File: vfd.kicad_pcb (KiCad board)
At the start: 2 copper layers, 100 x 34 mm, 45 parts, among them J1 I2C_IN, J2 I2C_OUT, Q1 BC857, Q2 BC847, Q3 BC857, Q4 BC847, U1 AP3012, U2 CH32V003F4U6, U3 AP3012, U4 74HCT541PW

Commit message: v0.2
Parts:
- removed TP5, TP6, TP7, TP8, TP9: TestPoint, TestPoint:TestPoint_Pad_D1.5mm
- added D3: LED, vfd:LED_0603_1608Metric, B.Cu at (19.0, 3.40)
- added JP1: A0, vfd:SolderJumper-2_P1.3mm_Open_TrianglePad1.0x1.5mm, B.Cu at (22.4, 7.35)
- added JP2: A1, vfd:SolderJumper-2_P1.3mm_Open_TrianglePad1.0x1.5mm, B.Cu at (25.0, 7.35)
- added JP3: A2, vfd:SolderJumper-2_P1.3mm_Open_TrianglePad1.0x1.5mm, B.Cu at (27.6, 7.35)
- added JP4: A3, vfd:SolderJumper-2_P1.3mm_Open_TrianglePad1.0x1.5mm, B.Cu at (30.1, 7.35)
- added JP5: A4, vfd:SolderJumper-2_P1.3mm_Open_TrianglePad1.0x1.5mm, B.Cu at (32.6, 7.35)
- added N2: OSHW, Symbol:OSHW-Logo_5.7x6mm_SilkScreen, B.Cu at (-40.0, 4.00)
- C1, C2, C3, C4, C5, C6: footprint Capacitor_SMD:C_0603_1608Metric -> vfd:C_0603_1608Metric
- D1, D2: footprint Diode_SMD:D_SOD-323 -> vfd:D_SOD-323
- J1, J2: footprint qwiic:1X04_1MM_RA_GND -> vfd:1X04_1MM_RA_GND
- L1, L2: footprint power-circuit:Inductor_MSC20FC -> vfd:Inductor_MSC20FC
- N1: value Housing -> Logo; footprint footprints:logo_nicolai -> vfd:logo_nicolai
- Q1, Q2, Q3, Q4: footprint Package_TO_SOT_SMD:SOT-23 -> vfd:SOT-23
- R1, R10, R11, R12, R13, R14, R2, R3, R4, R6, R8, R9: footprint Resistor_SMD:R_0603_1608Metric -> vfd:R_0603_1608Metric
- R5: value 1k -> 270; footprint Resistor_SMD:R_0603_1608Metric -> vfd:R_0603_1608Metric
- R7: value 92k82 -> 91k; footprint Resistor_SMD:R_0603_1608Metric -> vfd:R_0603_1608Metric
- TP1, TP2, TP3, TP4: footprint TestPoint:TestPoint_Pad_D1.5mm -> vfd:TestPoint_Pad_D1.5mm
- U1, U3: footprint Package_TO_SOT_SMD:SOT-23-5 -> vfd:SOT-23-5
- U2: footprint Package_DFN_QFN:QFN-20-1EP_3x3mm_P0.4mm_EP1.65x1.65mm -> vfd:QFN-20-1EP_3x3mm_P0.4mm_EP1.65x1.65mm
- U4: footprint Package_SO:TSSOP-20_4.4x6.5mm_P0.65mm -> vfd:TSSOP-20_4.4x6.5mm_P0.65mm
- U5: footprint hcs-12ss59t:HCS-12SS59T -> vfd:HCS-12SS59T
- moved J2 90.7 mm to (45.0, 6.62), turned to -90 degrees
- moved J1 90.4 mm to (45.0, -3.38), turned to -90 degrees
- moved R2 83.4 mm to (41.9, 3.95), turned to 180 degrees
- moved R1 81.9 mm to (41.9, 6.38), turned to 180 degrees
- moved C2 81.0 mm to (41.9, 2.40), turned to 180 degrees
- moved Q1 80.9 mm to (-39.9, -6.38)
- moved Q2 80.9 mm to (-43.9, -6.38)
- moved R10 80.9 mm to (-43.9, -3.38)
- moved R9 80.9 mm to (-39.9, -3.38)
- moved Q3 77.8 mm to (41.8, -6.40)
- moved Q4 77.8 mm to (37.8, -6.40)
- moved R12 77.8 mm to (40.3, -3.40)
- moved R13 77.8 mm to (36.6, -3.40)
- moved U2 72.0 mm to (37.0, 5.00), turned to -90 degrees
- moved R11 67.8 mm to (32.9, 2.27)
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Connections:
- Q1 pad 2: F+ -> +5V
- Q1 pad 3: +5V -> F+
- Q3 pad 2: F- -> +5V
- Q3 pad 3: +5V -> F-
- R5 pad 1: ~{CPU_RST} -> Net-(D3-A)
- R5 pad 2: +3.3V -> Net-(U2-PD7)
- U2 pad 1: ~{CPU_RST} -> Net-(U2-PD7)
- U4 pad 13: ~{CS} -> DIN
- U4 pad 14: ~{RST} -> CLK
- U4 pad 15: CLK -> ~{CS}
- U4 pad 16: DIN -> ~{RST}
- U4 pad 17: CLK_B -> CLK_A
- U4 pad 18: CLK_A -> CLK_B
- U4 pad 2: CLK_A_LV -> CLK_B_LV
- U4 pad 3: CLK_B_LV -> CLK_A_LV
- U4 pad 4: DIN_LV -> ~{RST_LV}
- U4 pad 5: CLK_LV -> ~{CS_LV}
- U4 pad 6: ~{RST_LV} -> CLK_LV
- U4 pad 7: ~{CS_LV} -> DIN_LV
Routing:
- net Net-(U2-PC7): track 34.6 -> 3.94 mm, vias 2 -> 0
- net +5V: track 123.3 -> 99.8 mm, vias 2 -> 4
- net SWIO: track 26.9 -> 4.05 mm
- net DIN_LV: track 7.92 -> 27.6 mm, vias 0 -> 2
- net Net-(JP5-A): track 22.0 -> 3.24 mm
- net CLK_LV: track 8.69 -> 25.9 mm, vias 0 -> 2
- net Net-(U2-PD7): track 0.00 -> 16.0 mm, vias 0 -> 2
- net ~{RST_LV}: track 9.45 -> 24.8 mm, vias 0 -> 2
- net Net-(JP4-A): track 18.7 -> 5.96 mm
- net 24V_ENABLE: track 47.2 -> 57.0 mm
- net ~{CS_LV}: track 15.6 -> 24.0 mm
- net CLK_A: track 83.9 -> 76.0 mm, vias 2 -> 0
- net DIN: track 11.9 -> 4.12 mm
- net CLK: track 12.2 -> 4.68 mm
- net Net-(JP3-A): track 15.6 -> 8.67 mm
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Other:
- board text added: "0 1 2 3 4"
- board text added: "Address"
- board text added: "G + E P"
- board text added: "HCS-12SS59T VFD DISPLAY"
- board text added: "https://product.nicolaielectronics.nl/hcs12ss59t"
- board text removed: "HCS-12SS59T VFD DISPLAY REV 0.1 7-2023"

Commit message: Version 0.2 final
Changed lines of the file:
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@@
     (tags "resistor")
     (property "Reference" "R5" (at 0 1.43 0 unlocked) (layer "B.SilkS")
-      (effects (font (size 1 1) (thickness 0.15)) (justify mirror))
+      (effects (font (size 0.8 0.8) (thickness 0.15)) (justify mirror))
     )
     (property "Value" "270" (at 0 -1.43 180 unlocked) (layer "B.Fab")
@@
     (fp_line (start 0.8 0.4125) (end -0.8 0.4125)
       (stroke (width 0.1) (type solid)) (layer "B.Fab"))
-    (fp_text user "${REFERENCE}" (at 0 0 360) (layer "B.Fab")
+    (fp_text user "${REFERENCE}" (at 0 0 0) (layer "B.Fab")
       (effects (font (size 0.4 0.4) (thickness 0.06)) (justify mirror))
     )
@@
     (descr "SOT, 3 Pin (https://www.jedec.org/system/files/docs/to-236h.pdf variant AB), generated with kicad-footprint-generator ipc_gullwing_generator.py")
     (tags "SOT TO_SOT_SMD")
-    (property "Reference" "Q1" (at 2.7 0 90) (layer "B.SilkS")
+    (property "Reference" "Q1" (at -0.075 -2.325 180) (layer "B.SilkS")
       (effects (font (size 0.8 0.8) (thickness 0.15)) (justify mirror))
     )
@@
     (descr "TSSOP, 20 Pin (JEDEC MO-153 Var AC https://www.jedec.org/document_search?search_api_views_fulltext=MO-153), generated with kicad-footprint-generator ipc_gullwing_generator.py")
     (tags "TSSOP SO")
-    (property "Reference" "U4" (at 0 4.2 -90 unlocked) (layer "B.SilkS")
+    (property "Reference" "U4" (at 0 4.2 90 unlocked) (layer "B.SilkS")
       (effects (font (size 0.8 0.8) (thickness 0.15)) (justify mirror))
     )
@@
     (descr "QFN, 20 Pin (https://www.analog.com/media/en/technical-documentation/data-sheets/3553fc.pdf#page=34), generated with kicad-footprint-generator ipc_noLead_generator.py")
     (tags "QFN NoLead")
-    (property "Reference" "U2" (at 0 2.82 90) (layer "B.SilkS")
+    (property "Reference" "U2" (at 0 -2.8 -90) (layer "B.SilkS")
       (effects (font (size 0.8 0.8) (thickness 0.15)) (justify mirror))
     )
@@
     (tags "Logo OSHW")
     (property "Reference" "N2" (at 0 0 0 unlocked) (layer "B.SilkS") hide
-      (effects (font (size 1 1) (thickness 0.15)) (justify mirror))
+      (effects (font (size 0.8 0.8) (thickness 0.15)) (justify mirror))
     )
     (property "Value" "OSHW" (at 0.75 0 0 unlocked) (layer "B.Fab") hide
@@
     (tags "LED")
     (property "Reference" "D3" (at 0 1.43 0 unlocked) (layer "B.SilkS")
-      (effects (font (size 1 1) (thickness 0.15)) (justify mirror))
+      (effects (font (size 0.8 0.8) (thickness 0.15)) (justify mirror))
     )
     (property "Value" "LED" (at 0 -1.43 180 unlocked) (layer "B.Fab")
@@
     (fp_line (start 0.8 0.4) (end 0.8 -0.4)
       (stroke (width 0.1) (type solid)) (layer "B.Fab"))
-    (fp_text user "${REFERENCE}" (at 0 0 360) (layer "B.Fab")
+    (fp_text user "${REFERENCE}" (at 0 0 0) (layer "B.Fab")
       (effects (font (size 0.4 0.4) (thickness 0.06)) (justify mirror))
     )
@@
     (descr "SOT, 3 Pin (https://www.jedec.org/system/files/docs/to-236h.pdf variant AB), generated with kicad-footprint-generator ipc_gullwing_generator.py")
     (tags "SOT TO_SOT_SMD")
-    (property "Reference" "Q2" (at -2.825 0 90) (layer "B.SilkS")
+    (property "Reference" "Q2" (at 0.025 -2.225 0) (layer "B.SilkS")
       (effects (font (size 0.8 0.8) (thickness 0.15)) (justify mirror))
     )
@@
     (descr "SOT, 3 Pin (https://www.jedec.org/system/files/docs/to-236h.pdf variant AB), generated with kicad-footprint-generator ipc_gullwing_generator.py")
     (tags "SOT TO_SOT_SMD")
-    (property "Reference" "Q3" (at 2.34 2.38 0) (layer "B.SilkS")
+    (property "Reference" "Q3" (at -0.025 -2.3 0) (layer "B.SilkS")
       (effects (font (size 0.8 0.8) (thickness 0.15)) (justify mirror))
     )
@@
     (descr "SOT, 3 Pin (https://www.jedec.org/system/files/docs/to-236h.pdf variant AB), generated with kicad-footprint-generator ipc_gullwing_generator.py")
     (tags "SOT TO_SOT_SMD")
-    (property "Reference" "Q4" (at -2.85 -1.875 0) (layer "B.SilkS")
+    (property "Reference" "Q4" (at -0.025 -2.3 0) (layer "B.SilkS")
       (effects (font (size 0.8 0.8) (thickness 0.15)) (justify mirror))
     )
@@
   (via (at 13.15 4.1) (size 0.6) (drill 0.3) (layers "F.Cu" "B.Cu") (free) (net 29))
   (via (at -48 -14.8) (size 3.5) (drill 3) (layers "F.Cu" "B.Cu") (free) (net 29))
-  (via (at -43.175 -8.525) (size 0.6) (drill 0.3) (layers "F.Cu" "B.Cu") (free) (net 29))
+  (via (at -45.2 -8.7) (size 0.6) (drill 0.3) (layers "F.Cu" "B.Cu") (free) (net 29))
   (via (at 1 4.425) (size 0.6) (drill 0.3) (layers "F.Cu" "B.Cu") (free) (net 29))
   (via (at -9.4 -10.5) (size 0.6) (drill 0.3) (layers "F.Cu" "B.Cu") (free) (net 29))

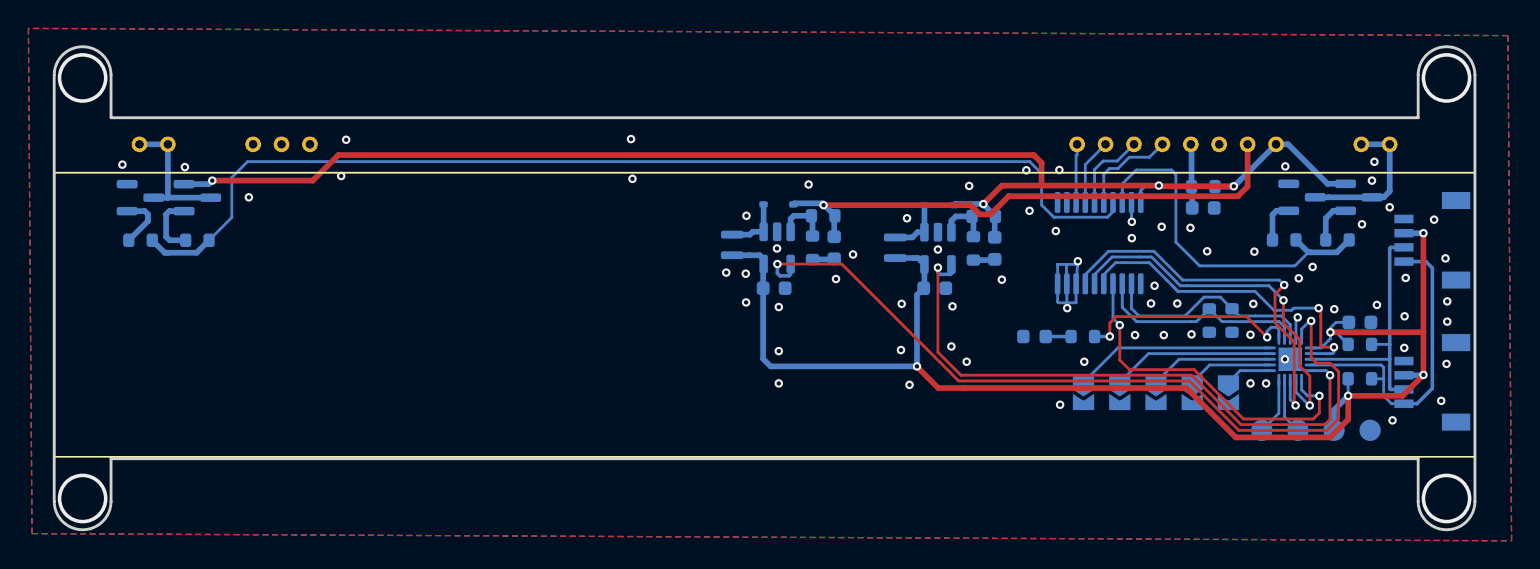
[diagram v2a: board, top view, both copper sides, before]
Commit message: Make inductor pads bigger, make vfd pads and holes larger
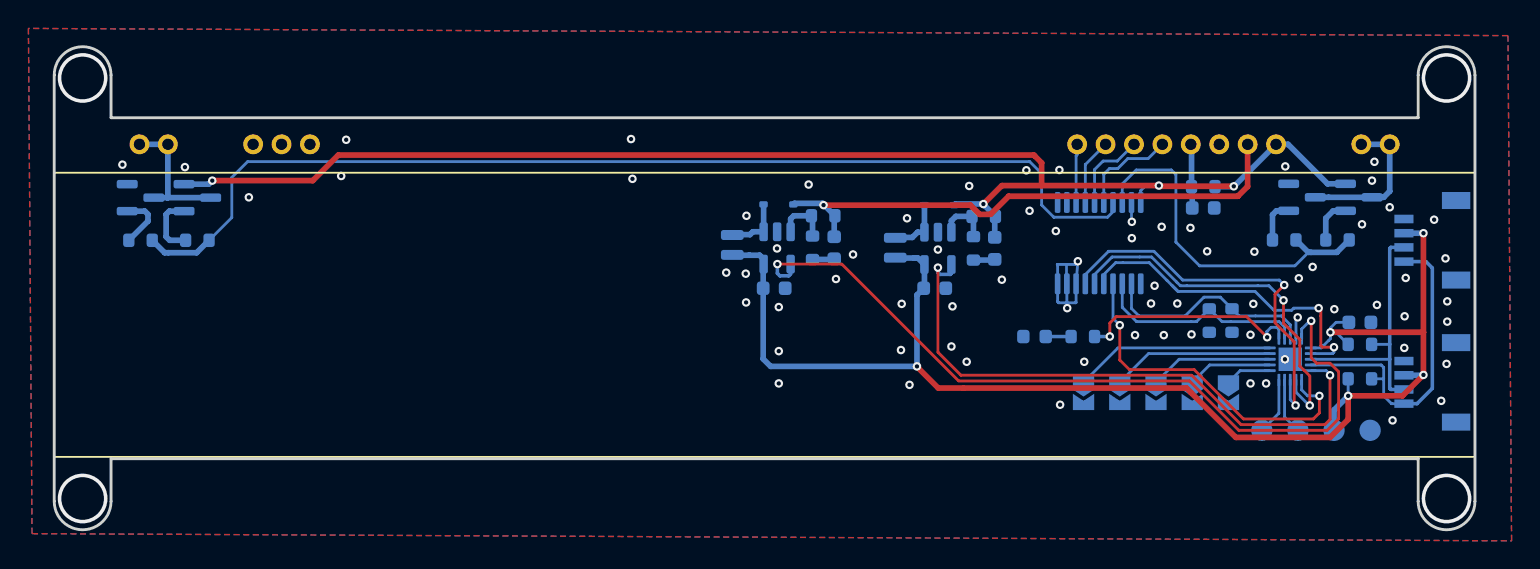
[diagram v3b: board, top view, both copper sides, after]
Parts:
- L1, L2: footprint vfd:Inductor_MSC20FC -> vfd:Inductor_201610

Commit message: Revision 1.0 final
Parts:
- added J3: I2C_HDR, Connector_PinHeader_2.54mm:PinHeader_1x04_P2.54mm_Vertical, B.Cu at (29.9, 10.2)
- added N3: Logo, vfd:logo_nicolai, F.Cu at (-20.0, 0.00)
- TP1: value TestPoint -> SWIO
- TP2: value TestPoint -> EXT
- TP3: value TestPoint -> GND
- TP4: value TestPoint -> 3.3v
- moved N2 7.08 mm to (-46.0, 7.75)
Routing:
- net SDA: track 18.7 -> 42.1 mm, vias 0 -> 1
- net SCL: track 22.7 -> 42.6 mm, vias 0 -> 1
- net +5V: track 99.8 -> 119.6 mm, vias 4 -> 7
- net +3.3V: track 98.8 -> 101.3 mm
- net CLK_A: track 76.0 -> 78.0 mm
- net 24V_ENABLE: track 57.0 -> 56.3 mm
- net 5V_ENABLE: track 42.6 -> 41.9 mm
- net GND: vias 77 -> 85
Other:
- board text added: "1.0"
- board text added: "GND 3.3v SDA SCL"
- board text removed: "https://product.nicolaielectronics.nl/hcs12ss59t"
